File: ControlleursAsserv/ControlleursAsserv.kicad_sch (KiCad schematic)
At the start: 33 parts, among them J1 I2C1_5, J2 I2C2_5, J3 CAN1, J4 CAN2, J5 In App Prog, J6 DEBUG, SW1 RESET, SW2 BOOT0, U1 STM32G474RETx, U2 AMS1117-3.3, U3 MCP2558FD-xSN

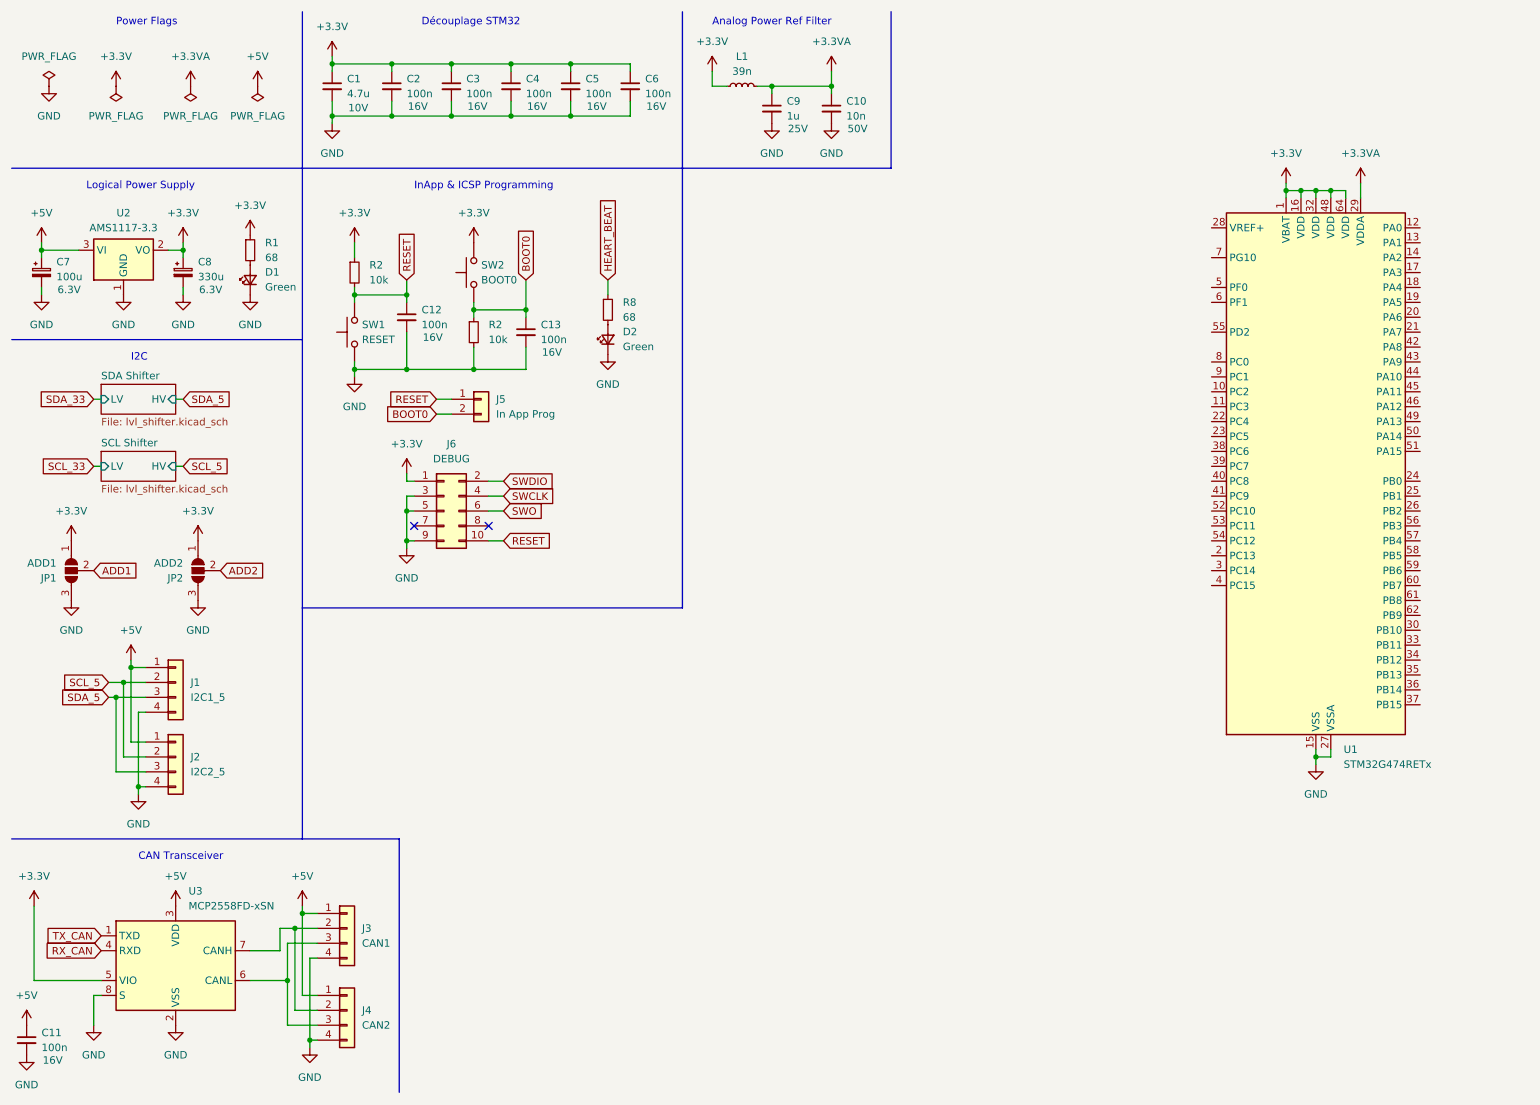
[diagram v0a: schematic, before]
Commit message: Upgrade base schematics
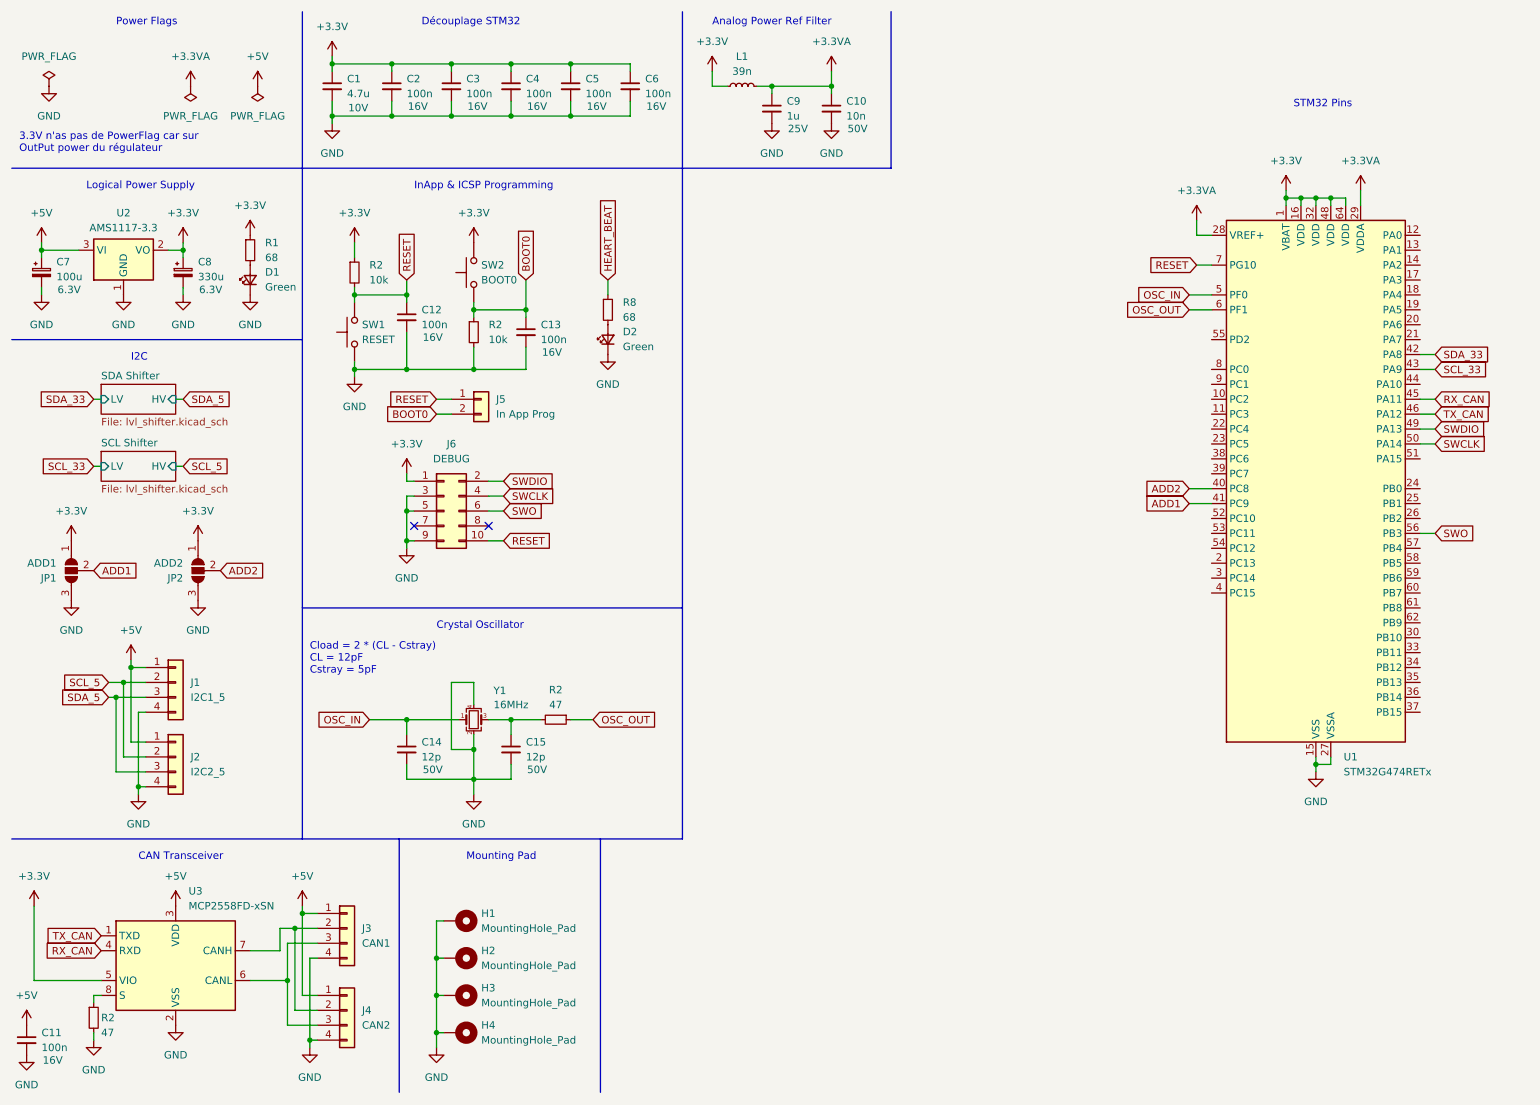
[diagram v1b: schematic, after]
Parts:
- added C14, C15: 12p, Capacitor_SMD:C_0402_1005Metric_Pad0.74x0.62mm_HandSolder, symbol Device:C_Small
- added H1, H2, H3, H4: MountingHole_Pad, MountingHole:MountingHole_3.2mm_M3_Pad_Via, symbol Mechanical:MountingHole_Pad
- added R2 (x2): 47, Resistor_SMD:R_0402_1005Metric_Pad0.72x0.64mm_HandSolder, symbol Device:R_Small
- added Y1: 16MHz, Crystal:Crystal_SMD_3225-4Pin_3.2x2.5mm_HandSoldering, symbol Device:Crystal_GND24_Small
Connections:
- net +3.3VA: now also U1.28 (VREF+)
- net ADD1: now also U1.41 (PC9)
- net ADD2: now also U1.40 (PC8)
- net GND: now also C14.2, C15.2, H1.1, H2.1, H3.1, H4.1, R2.2, Y1.2, Y1.4; no longer U3.8 (S)
- net RESET: now also U1.7 (PG10)
- net RX_CAN: now also U1.45 (PA11)
- net SCL_33: now also U1.43 (PA9)
- net SDA_33: now also U1.42 (PA8)
- net SWCLK: now also U1.50 (PA14)
- net SWDIO: now also U1.49 (PA13)
- net SWO: now also U1.56 (PB3)
- net TX_CAN: now also U1.46 (PA12)
- net OSC_IN: now reaches U1.5 (PF0)
- net OSC_IN: now also C14.1, Y1.1
- net OSC_OUT: now reaches U1.6 (PF1)
- net OSC_OUT: now also R2.1
- new net: R2.1, U3.8 (S)
- new net: C15.1, R2.2, Y1.3
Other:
- note added: "3.3V n'as pas de PowerFlag car sur OutPut power du régulateur"
- note added: "Cload = 2 * (CL - Cstray) CL = 12pF Cstray = 5pF"
- note added: "Crystal Oscillator"
- note added: "Mounting Pad"
- note added: "STM32 Pins"
- moved on the sheet: U1

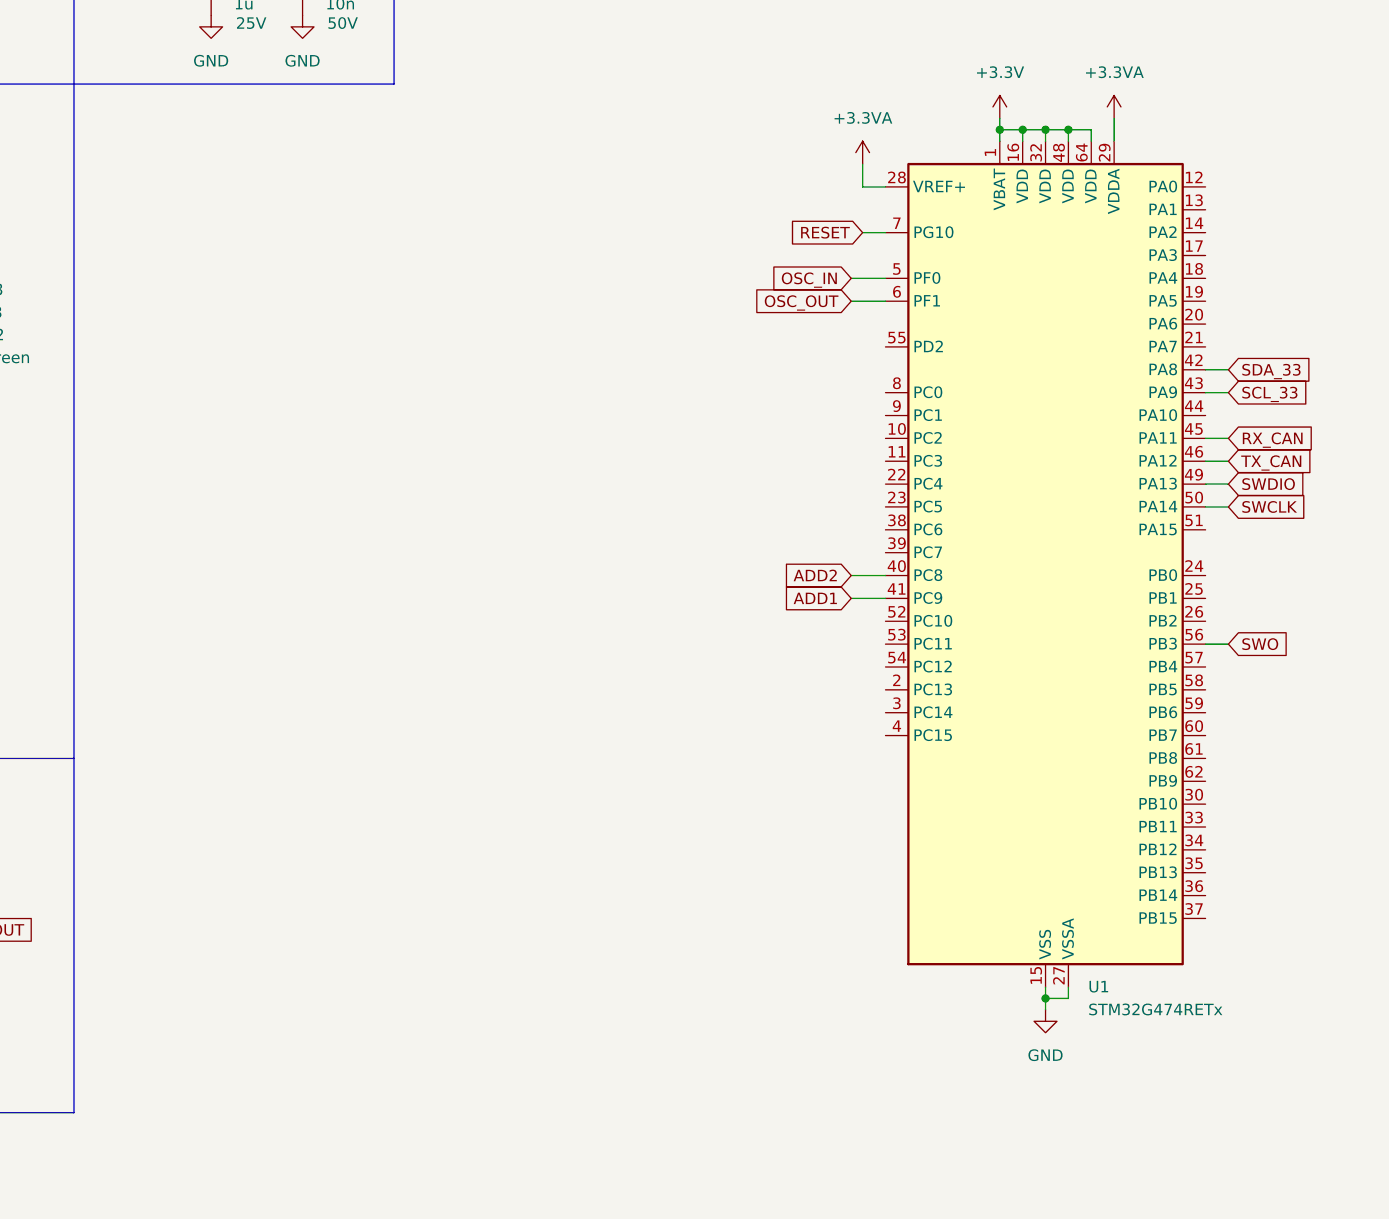
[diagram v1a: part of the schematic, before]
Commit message: Add coders & motors interface
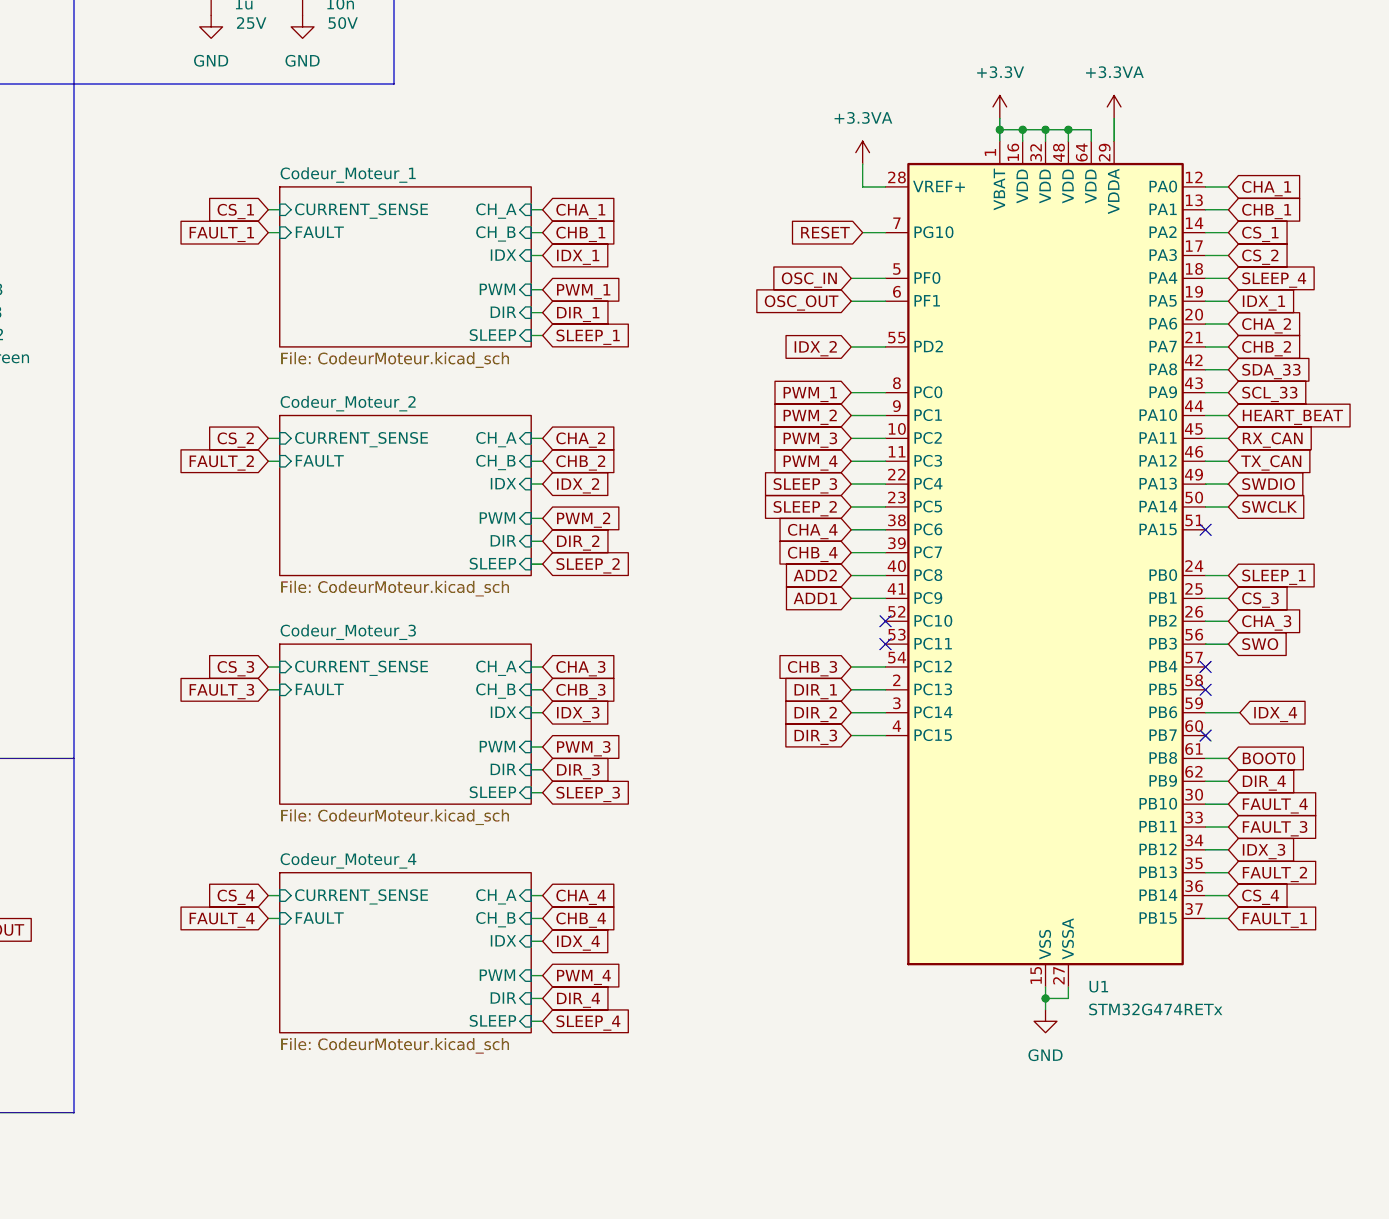
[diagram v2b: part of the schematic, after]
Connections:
- net BOOT0: now also U1.61 (PB8)
- net HEART_BEAT: now also U1.44 (PA10)
- net PWM_3: now reaches U1.10 (PC2)
- net PWM_4: now reaches U1.11 (PC3)
- net CHA_1: now reaches U1.12 (PA0)
- net CHB_1: now reaches U1.13 (PA1)
- net CS_1: now reaches U1.14 (PA2)
- net CS_2: now reaches U1.17 (PA3)
- net SLEEP_4: now reaches U1.18 (PA4)
- net IDX_1: now reaches U1.19 (PA5)
- net DIR_1: now reaches U1.2 (PC13)
- net CHA_2: now reaches U1.20 (PA6)
- net CHB_2: now reaches U1.21 (PA7)
- net SLEEP_3: now reaches U1.22 (PC4)
- net SLEEP_2: now reaches U1.23 (PC5)
- net SLEEP_1: now reaches U1.24 (PB0)
- net CS_3: now reaches U1.25 (PB1)
- net CHA_3: now reaches U1.26 (PB2)
- net DIR_2: now reaches U1.3 (PC14)
- net FAULT_4: now reaches U1.30 (PB10)
- net FAULT_3: now reaches U1.33 (PB11)
- net IDX_3: now reaches U1.34 (PB12)
- net FAULT_2: now reaches U1.35 (PB13)
- net CS_4: now reaches U1.36 (PB14)
- net FAULT_1: now reaches U1.37 (PB15)
- net CHA_4: now reaches U1.38 (PC6)
- net CHB_4: now reaches U1.39 (PC7)
- net DIR_3: now reaches U1.4 (PC15)
- net CHB_3: now reaches U1.54 (PC12)
- net IDX_2: now reaches U1.55 (PD2)
- net IDX_4: now reaches U1.59 (PB6)
- net DIR_4: now reaches U1.62 (PB9)
- net PWM_1: now reaches U1.8 (PC0)
- net PWM_2: now reaches U1.9 (PC1)
- no-connect marks 2 -> 8
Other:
- added sheet Codeur_Moteur_1 (CodeurMoteur.kicad_sch)
- added sheet Codeur_Moteur_2 (CodeurMoteur.kicad_sch)
- added sheet Codeur_Moteur_3 (CodeurMoteur.kicad_sch)
- added sheet Codeur_Moteur_4 (CodeurMoteur.kicad_sch)
